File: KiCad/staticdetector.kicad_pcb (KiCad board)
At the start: 2 copper layers, 35 x 77.5 mm, 17 parts, among them J1 Conn_01x04, Q1 Q_NMOS_GDS_2SK4033, Q2 Q_NPN_BEC_2PD601ART, Q3 Q_NPN_BCE_2SCR533P, SW1 SW_Push

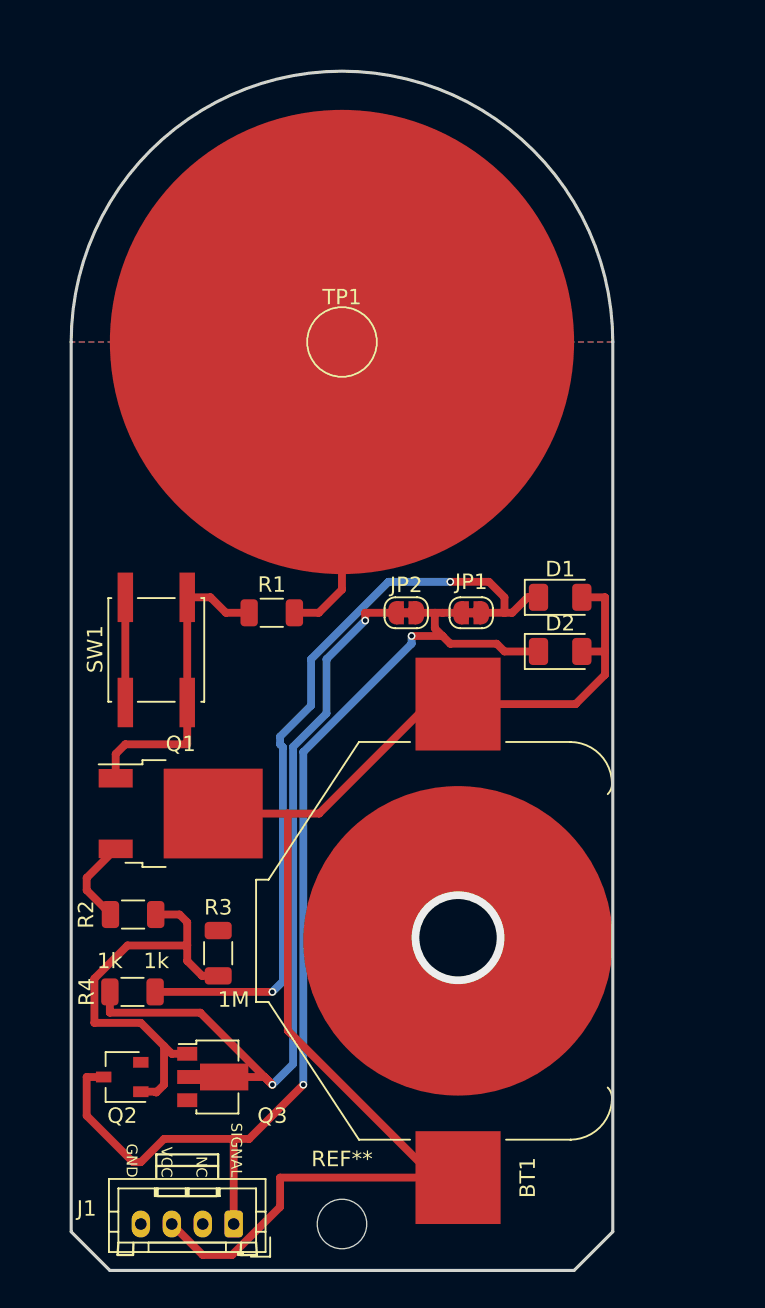
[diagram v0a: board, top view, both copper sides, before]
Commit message: change file to OPAMP version
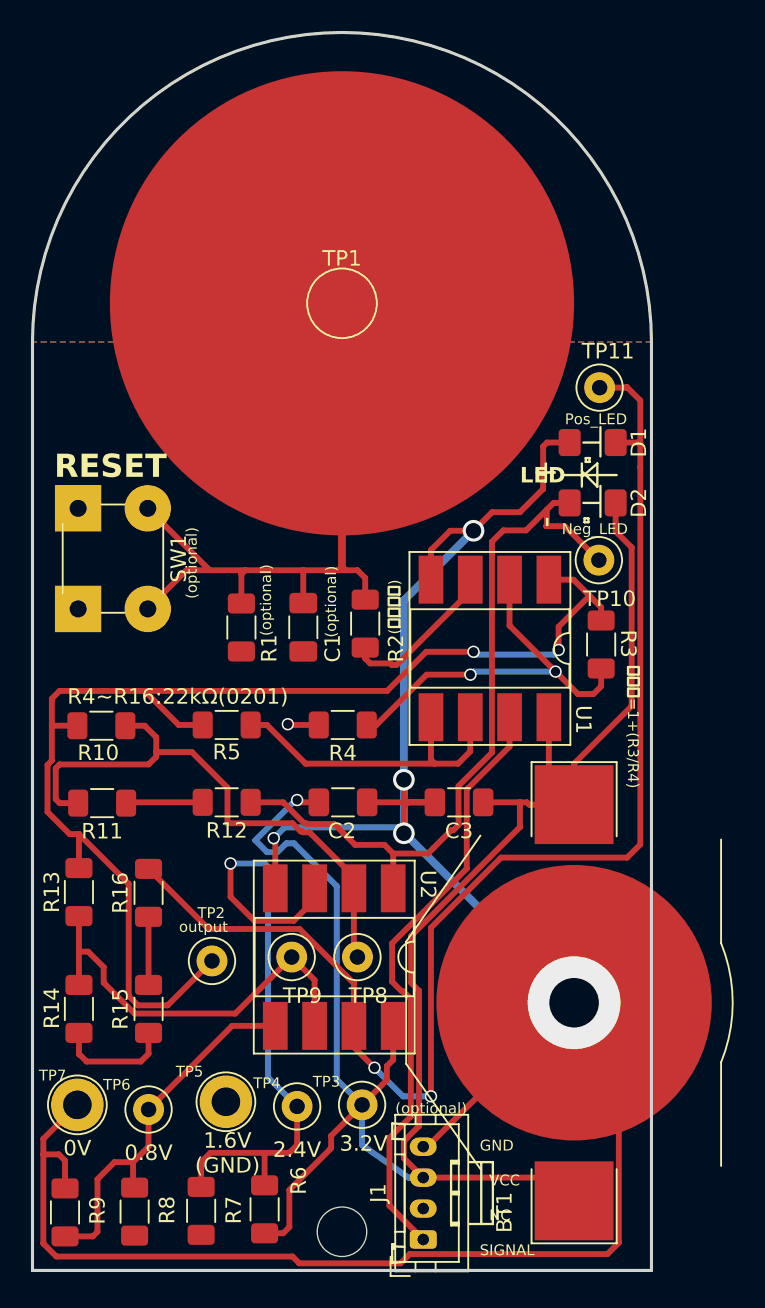
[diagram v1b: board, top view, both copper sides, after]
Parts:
- removed JP1, JP2: Jumper_2_Bridged, Jumper:SolderJumper-2_P1.3mm_Bridged_RoundedPad1.0x1.5mm
- removed Q1: Q_NMOS_GDS_2SK4033, Package_TO_SOT_SMD:TO-252-2
- removed Q2: Q_NPN_BEC_2PD601ART, Package_TO_SOT_SMD:SOT-23W
- removed Q3: Q_NPN_BCE_2SCR533P, Package_TO_SOT_SMD:SOT-89-3
- added C1: 100n, Capacitor_SMD:C_1206_3216Metric_Pad1.33x1.80mm_HandSolder, F.Cu at (127.5, 78.4)
- added C2: 100n, Capacitor_SMD:C_1206_3216Metric_Pad1.33x1.80mm_HandSolder, F.Cu at (130.1, 89.8)
- added C3: 100n, Capacitor_SMD:C_1206_3216Metric_Pad1.33x1.80mm_HandSolder, F.Cu at (137.6, 89.8)
- added R10: 22k, Resistor_SMD:R_1206_3216Metric_Pad1.30x1.75mm_HandSolder, F.Cu at (114.5, 84.8)
- added R11: 22k, Resistor_SMD:R_1206_3216Metric_Pad1.30x1.75mm_HandSolder, F.Cu at (114.5, 89.8)
- added R12: 22k, Resistor_SMD:R_1206_3216Metric_Pad1.30x1.75mm_HandSolder, F.Cu at (122.5, 89.8)
- added R13: 22k, Resistor_SMD:R_1206_3216Metric_Pad1.30x1.75mm_HandSolder, F.Cu at (113.0, 95.5)
- added R14: 22k, Resistor_SMD:R_1206_3216Metric_Pad1.30x1.75mm_HandSolder, F.Cu at (113.0, 103.1)
- added R15: 22k, Resistor_SMD:R_1206_3216Metric_Pad1.30x1.75mm_HandSolder, F.Cu at (117.5, 103.1)
- added R16: 22k, Resistor_SMD:R_1206_3216Metric_Pad1.30x1.75mm_HandSolder, F.Cu at (117.5, 95.6)
- added R5: 22k, Resistor_SMD:R_1206_3216Metric_Pad1.30x1.75mm_HandSolder, F.Cu at (122.5, 84.8)
- added R6: 22k, Resistor_SMD:R_1206_3216Metric_Pad1.30x1.75mm_HandSolder, F.Cu at (125.0, 116.0)
- added R7: 22k, Resistor_SMD:R_1206_3216Metric_Pad1.30x1.75mm_HandSolder, F.Cu at (120.9, 116.2)
- added R8: 22k, Resistor_SMD:R_1206_3216Metric_Pad1.30x1.75mm_HandSolder, F.Cu at (116.6, 116.2)
- added R9: 22k, Resistor_SMD:R_1206_3216Metric_Pad1.30x1.75mm_HandSolder, F.Cu at (112.1, 116.2)
- added TP10: output, TestPoint:TestPoint_Loop_D1.80mm_Drill1.0mm_Beaded, F.Cu at (146.6, 74.1)
- added TP11: output, TestPoint:TestPoint_Loop_D1.80mm_Drill1.0mm_Beaded, F.Cu at (146.7, 63.0)
- added TP2: output, TestPoint:TestPoint_Loop_D1.80mm_Drill1.0mm_Beaded, F.Cu at (121.6, 100.0)
- added TP3: 3.2V, TestPoint:TestPoint_Loop_D1.80mm_Drill1.0mm_Beaded, F.Cu at (131.3, 109.3)
- added TP4: 2.4V, TestPoint:TestPoint_Loop_D1.80mm_Drill1.0mm_Beaded, F.Cu at (127.1, 109.4)
- added TP5: 1.6V, TestPoint:TestPoint_Loop_D2.50mm_Drill1.85mm, F.Cu at (122.5, 109.1)
- added TP6: 0.8V, TestPoint:TestPoint_Loop_D1.80mm_Drill1.0mm_Beaded, F.Cu at (117.5, 109.6)
- added TP7: 0V, TestPoint:TestPoint_Loop_D2.50mm_Drill1.85mm, F.Cu at (112.9, 109.3)
- added TP8: 2.4V, TestPoint:TestPoint_Loop_D1.80mm_Drill1.0mm_Beaded, F.Cu at (131.0, 99.8)
- added TP9: 0.8V, TestPoint:TestPoint_Loop_D1.80mm_Drill1.0mm_Beaded, F.Cu at (126.8, 99.8)
- added U1: AD8506, Package_DIP:DIP-8_W8.89mm_SMDSocket_LongPads, F.Cu at (139.6, 79.8)
- added U2: AD8506, Package_DIP:DIP-8_W8.89mm_SMDSocket_LongPads, F.Cu at (129.5, 99.8)
- BT1: footprint Battery:BatteryHolder_Keystone_3008_1x2450 -> Battery:BatteryHolder_Keystone_3002_1x2032
- D1: value LED -> Negative Vf=3V; footprint LED_SMD:LED_1206_3216Metric -> LED_SMD:LED_1206_3216Metric_Pad1.42x1.75mm_HandSolder
- D2: value LED -> Positive Vf=2V; footprint LED_SMD:LED_1206_3216Metric -> LED_SMD:LED_1206_3216Metric_Pad1.42x1.75mm_HandSolder
- J1: value Conn_01x04 -> HY_CONN
- R1: value 10M -> 20M; footprint Resistor_SMD:R_1206_3216Metric -> Resistor_SMD:R_1206_3216Metric_Pad1.30x1.75mm_HandSolder
- R2: value 1k -> 100k; footprint Resistor_SMD:R_1206_3216Metric -> Resistor_SMD:R_1206_3216Metric_Pad1.30x1.75mm_HandSolder
- R3: footprint Resistor_SMD:R_1206_3216Metric -> Resistor_SMD:R_1206_3216Metric_Pad1.30x1.75mm_HandSolder
- R4: value 1k -> 22k; footprint Resistor_SMD:R_1206_3216Metric -> Resistor_SMD:R_1206_3216Metric_Pad1.30x1.75mm_HandSolder
- SW1: footprint Button_Switch_SMD:SW_SPST_EVQQ2 -> Button_Switch_THT:SW_PUSH_6mm
- moved R3 31.8 mm to (146.8, 79.5)
- moved R2 24.1 mm to (131.5, 78.2), turned to -90 degrees
- moved R4 22.0 mm to (130.1, 84.8)
- moved J1 12.3 mm to (135.2, 118.0), turned to 90 degrees
- moved D1 10.2 mm to (146.2, 66.5)
- moved D2 9.83 mm to (146.2, 70.4)
- moved SW1 9.17 mm to (117.5, 70.8), turned to -90 degrees
- moved BT1 8.50 mm to (145.0, 102.7), turned to -90 degrees
- moved TP1 2.50 mm to (130.0, 57.5)
- moved R1 2.18 mm to (123.5, 78.5), turned to -90 degrees
- moved REF** 0.50 mm to (130.0, 117.5)
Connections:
- BT1 pad 1: BATT -> +VDC
- BT1 pad 2: GND -> -VDC
- D1 pad 1: Net-(D1-K) -> -VDC
- D1 pad 2: BATT -> Net-(D1-A)
- D2 pad 2: BATT -> +VDC
- J1 pad 1: Net-(D2-K) -> Net-(J1-Pin_1)
- J1 pad 3: BATT -> +VDC
- J1 pad 4: GND -> -VDC
- R1 pad 1: Net-(Q1-G) -> Net-(C1-Pad1)
- R1 pad 2: Net-(R1-Pad2) -> GND
- R2 pad 1: Net-(Q2-B) -> Net-(C1-Pad1)
- R3 pad 1: Net-(Q2-B) -> Net-(U1A--)
- R3 pad 2: GND -> Net-(R10-Pad1)
- R4 pad 1: Net-(D1-K) -> Net-(U1A--)
- R4 pad 2: Net-(JP2-A) -> GND
- SW1 pad 1: GND -> Net-(C1-Pad1)
- SW1 pad 2: Net-(Q1-G) -> GND
- TP1 pad 1: Net-(R1-Pad2) -> Net-(C1-Pad1)
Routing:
- net -VDC: track 0.00 -> 161.4 mm, vias 0 -> 5
- net +VDC: track 0.00 -> 124.2 mm, vias 0 -> 1
- net BATT: track 88.5 -> 0.00 mm
- net Net-(D1-A): track 0.00 -> 86.7 mm, vias 0 -> 2
- net Net-(R10-Pad1): track 0.00 -> 81.0 mm, vias 0 -> 2
- net Net-(JP2-A): track 54.4 -> 0.00 mm, vias 2 -> 0
- net Net-(D1-K): track 50.4 -> 0.00 mm, vias 2 -> 0
- net Net-(C1-Pad1): track 0.00 -> 42.3 mm
- net Net-(U2A-+): track 0.00 -> 41.2 mm, vias 0 -> 1
- net Net-(J1-Pin_1): track 0.00 -> 38.9 mm
- net Net-(U2A--): track 0.00 -> 36.7 mm
- net Net-(Q2-B): track 27.9 -> 0.00 mm
- net Net-(U2B--): track 0.00 -> 27.0 mm
- net Net-(U1A--): track 0.00 -> 25.7 mm, vias 0 -> 2
- net Net-(U2B-+): track 0.00 -> 24.3 mm
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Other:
- board size 35 x 77.5 mm -> 40 x 80 mm
- board text added: "(optional)"
- board text added: "(保護抵抗)"
- board text added: "- +"
- board text added: "0.8V"
- board text added: "0.8V feedback"
- board text added: "0V"
- board text added: "1.6V (GND)"
- board text added: "2.4V"
- board text added: "2.4V feedback"
- board text added: "3.2V"
- board text added: "GND VCC NC SIGNAL"
- board text added: "LED"
- board text added: "Neg_LED"
- board text added: "OPENFORCE 静電気ディテクターOPAMP版 Ver.20230330"
- board text added: "Pos_LED"
- board text added: "R4~R16:22kΩ(0201)"
- board text added: "RESET"
- board text added: "output"
- board text added: "増幅率=1+(R3/R4)"
- board text removed: "OPENFORCE 静電気ディテクター Ver.20230222"
- board text removed: "SIGNAL NC VCC GND"
